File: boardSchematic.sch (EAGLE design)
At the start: 61 parts, among them IC2 TP4056, Q1 BC817-40SMD, Q2 BC817-40SMD, Q3 BC817-40SMD

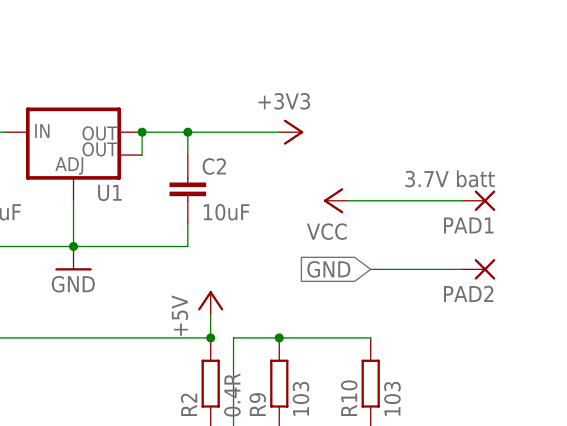
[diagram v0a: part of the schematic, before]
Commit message: Added on/off switch
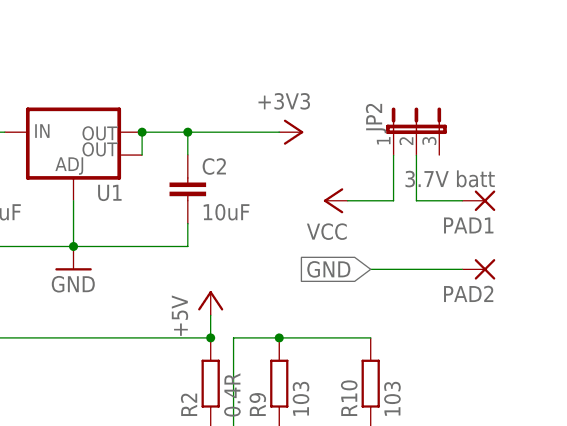
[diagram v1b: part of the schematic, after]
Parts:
- added JP2: (no value), jumper:JP2E
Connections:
- new net N$28: JP2.2, PAD1.P
- net VCC: now also JP2.1; no longer PAD1.P
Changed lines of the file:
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@@
 <part name="R24" library="rcl" deviceset="R-EU_" device="R0805" value="103"/>
 <part name="R27" library="rcl" deviceset="R-EU_" device="R0805" value="103"/>
+<part name="JP2" library="jumper" deviceset="JP2E" device=""/>
 </parts>
 <sheets>
@@
 <instance part="R24" gate="G$1" x="109.22" y="-129.54" rot="R90"/>
 <instance part="R27" gate="G$1" x="172.72" y="-132.08" rot="R90"/>
+<instance part="JP2" gate="1" x="325.12" y="-7.62"/>
 </instances>
 <busses>
@@
 <net name="VCC" class="0">
 <segment>
-<pinref part="P+1" gate="VCC" pin="VCC"/>
-<pinref part="PAD1" gate="1" pin="P"/>
-<wire x1="317.5" y1="-15.24" x2="330.2" y2="-15.24" width="0.1524" layer="91"/>
-</segment>
-<segment>
 <pinref part="U1" gate="G$1" pin="IN"/>
 <pinref part="C1" gate="G$1" pin="1"/>
@@
 <junction x="68.58" y="-99.06"/>
 </segment>
+<segment>
+<pinref part="P+1" gate="VCC" pin="VCC"/>
+<pinref part="JP2" gate="1" pin="1"/>
+<wire x1="317.5" y1="-15.24" x2="322.58" y2="-15.24" width="0.1524" layer="91"/>
+<wire x1="322.58" y1="-15.24" x2="322.58" y2="-10.16" width="0.1524" layer="91"/>
+</segment>
 </net>
 <net name="+5V" class="0">
@@
 </segment>
 </net>
+<net name="N$28" class="0">
+<segment>
+<pinref part="JP2" gate="1" pin="2"/>
+<wire x1="325.12" y1="-10.16" x2="325.12" y2="-15.24" width="0.1524" layer="91"/>
+<pinref part="PAD1" gate="1" pin="P"/>
+<wire x1="325.12" y1="-15.24" x2="330.2" y2="-15.24" width="0.1524" layer="91"/>
+</segment>
+</net>

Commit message: First guess of routing
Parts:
- removed LED1: RD, led:LEDSML0805
- removed LED2, LED4: GR, led:LEDSML0805
- removed R10, R9: 103, rcl:R-EU_R0805
- removed R19, R20, R21, R23: 102, rcl:R-EU_R0805
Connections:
- removed net N$1: Q2.B, R21.2
- removed net N$10: IC2.STDBY, LED2.C
- removed net N$2: LED1.A, R9.1
- removed net N$21: Q3.B, R23.2
- removed net N$26: LED4.A, R20.1
- removed net N$29: MEGA328.PD4(T0/XCK/PCINT20), R20.2
- removed net N$4: Q1.B, R19.2
- removed net N$6: LED2.A, R10.1
- removed net N$8: IC2.CHRG, LED1.C
- net BZR: now also Q3.B; no longer R23.1
- net GND: no longer LED4.C
- net GR: now also Q2.B; no longer R21.1
- net N$14: no longer R10.2, R9.2
- net RD: now also Q1.B; no longer R19.1
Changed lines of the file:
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@@
 <part name="R2" library="rcl" deviceset="R-EU_" device="R1210W" value="0.4R"/>
 <part name="R8" library="rcl" deviceset="R-EU_" device="R0805" value="122"/>
-<part name="R9" library="rcl" deviceset="R-EU_" device="R0805" value="103"/>
-<part name="R10" library="rcl" deviceset="R-EU_" device="R0805" value="103"/>
 <part name="C4" library="rcl" deviceset="C-EU" device="C1210" value="10uF"/>
 <part name="C5" library="rcl" deviceset="C-EU" device="C1210" value="10uF"/>
-<part name="LED1" library="led" deviceset="LED" device="SML0805" value="RD"/>
-<part name="LED2" library="led" deviceset="LED" device="SML0805" value="GR"/>
 <part name="GND5" library="supply1" deviceset="GND" device=""/>
 <part name="RF" library="pinhead" deviceset="PINHD-2X4" device=""/>
@@
 <part name="R14" library="rcl" deviceset="R-US_" device="R0805" value="103"/>
 <part name="BEACON" library="frankduerr" deviceset="MOD-NRF8001" device="MOD-NRF8001"/>
-<part name="R20" library="rcl" deviceset="R-EU_" device="R0805" value="102"/>
-<part name="LED4" library="led" deviceset="LED" device="SML0805" value="GR"/>
-<part name="GND4" library="supply1" deviceset="GND" device=""/>
 <part name="LED3" library="led" deviceset="Z-POWER-LED" device=""/>
 <part name="LED5" library="led" deviceset="Z-POWER-LED" device=""/>
@@
 <part name="R17" library="rcl" deviceset="R-EU_" device="R1206" value="1R0"/>
 <part name="R18" library="rcl" deviceset="R-EU_" device="R1206" value="1R0"/>
-<part name="R19" library="rcl" deviceset="R-EU_" device="R0805" value="102"/>
-<part name="R21" library="rcl" deviceset="R-EU_" device="R0805" value="102"/>
 <part name="Q1" library="transistor-npn" deviceset="BC817*" device="SMD" technology="-40"/>
 <part name="Q2" library="transistor-npn" deviceset="BC817*" device="SMD" technology="-40"/>
@@
 <part name="P+2" library="supply1" deviceset="VCC" device=""/>
 <part name="SG1" library="buzzer" deviceset="F/HMB" device=""/>
-<part name="R23" library="rcl" deviceset="R-EU_" device="R0805" value="102"/>
 <part name="Q3" library="transistor-npn" deviceset="BC817*" device="SMD" technology="-40"/>
 <part name="U$2" library="SparkFun-AnalogIC" deviceset="LM393" device=""/>
@@
 <instance part="R2" gate="G$1" x="302.26" y="-35.56" rot="R90"/>
 <instance part="R8" gate="G$1" x="269.24" y="-66.04" rot="R90"/>
-<instance part="R9" gate="G$1" x="309.88" y="-35.56" rot="R90"/>
-<instance part="R10" gate="G$1" x="320.04" y="-35.56" rot="R90"/>
 <instance part="C4" gate="G$1" x="314.96" y="-66.04"/>
 <instance part="C5" gate="G$1" x="304.8" y="-66.04"/>
-<instance part="LED1" gate="G$1" x="309.88" y="-45.72"/>
-<instance part="LED2" gate="G$1" x="320.04" y="-45.72"/>
 <instance part="GND5" gate="1" x="264.16" y="-81.28"/>
 <instance part="RF" gate="A" x="139.7" y="-83.82"/>
@@
 <instance part="R14" gate="G$1" x="119.38" y="-83.82"/>
 <instance part="BEACON" gate="G$1" x="182.88" y="-33.02"/>
-<instance part="R20" gate="G$1" x="91.44" y="-43.18" rot="R180"/>
-<instance part="LED4" gate="G$1" x="101.6" y="-43.18" rot="R90"/>
-<instance part="GND4" gate="1" x="109.22" y="-48.26"/>
 <instance part="LED3" gate="G$1" x="22.86" y="-119.38"/>
 <instance part="LED5" gate="G$1" x="38.1" y="-119.38"/>
@@
 <instance part="R17" gate="G$1" x="53.34" y="-109.22" rot="R270"/>
 <instance part="R18" gate="G$1" x="68.58" y="-109.22" rot="R270"/>
-<instance part="R19" gate="G$1" x="12.7" y="-134.62"/>
-<instance part="R21" gate="G$1" x="12.7" y="-149.86"/>
 <instance part="Q1" gate="G$1" x="58.42" y="-134.62"/>
 <instance part="Q2" gate="G$1" x="27.94" y="-149.86"/>
@@
 <instance part="P+2" gate="VCC" x="53.34" y="-91.44"/>
 <instance part="SG1" gate="G$1" x="86.36" y="-111.76" rot="R270"/>
-<instance part="R23" gate="G$1" x="12.7" y="-142.24"/>
 <instance part="Q3" gate="G$1" x="81.28" y="-142.24"/>
 <instance part="U$2" gate="G1" x="139.7" y="-137.16"/>
@@
 <wire x1="167.64" y1="-30.48" x2="157.48" y2="-30.48" width="0.1524" layer="91"/>
 <label x="157.48" y="-30.48" size="1.778" layer="95"/>
-</segment>
-<segment>
-<pinref part="LED4" gate="G$1" pin="C"/>
-<pinref part="GND4" gate="1" pin="GND"/>
-<wire x1="109.22" y1="-43.18" x2="106.68" y2="-43.18" width="0.1524" layer="91"/>
-<wire x1="109.22" y1="-45.72" x2="109.22" y2="-43.18" width="0.1524" layer="91"/>
-<junction x="109.22" y="-43.18"/>
 </segment>
 <segment>
@@
 </segment>
 </net>
-<net name="N$2" class="0">
-<segment>
-<pinref part="LED1" gate="G$1" pin="A"/>
-<pinref part="R9" gate="G$1" pin="1"/>
-<wire x1="309.88" y1="-43.18" x2="309.88" y2="-40.64" width="0.1524" layer="91"/>
-</segment>
-</net>
-<net name="N$6" class="0">
-<segment>
-<pinref part="LED2" gate="G$1" pin="A"/>
-<pinref part="R10" gate="G$1" pin="1"/>
-<wire x1="320.04" y1="-43.18" x2="320.04" y2="-40.64" width="0.1524" layer="91"/>
-</segment>
-</net>
-<net name="N$8" class="0">
-<segment>
-<pinref part="IC2" gate="G$1" pin="CHRG"/>
-<pinref part="LED1" gate="G$1" pin="C"/>
-<wire x1="302.26" y1="-50.8" x2="309.88" y2="-50.8" width="0.1524" layer="91"/>
-</segment>
-</net>
-<net name="N$10" class="0">
-<segment>
-<pinref part="IC2" gate="G$1" pin="STDBY"/>
-<pinref part="LED2" gate="G$1" pin="C"/>
-<wire x1="302.26" y1="-53.34" x2="320.04" y2="-53.34" width="0.1524" layer="91"/>
-<wire x1="320.04" y1="-53.34" x2="320.04" y2="-50.8" width="0.1524" layer="91"/>
-</segment>
-</net>
 <net name="N$14" class="0">
 <segment>
-<pinref part="R10" gate="G$1" pin="2"/>
-<pinref part="R9" gate="G$1" pin="2"/>
-<wire x1="320.04" y1="-30.48" x2="309.88" y2="-30.48" width="0.1524" layer="91"/>
-<wire x1="309.88" y1="-30.48" x2="304.8" y2="-30.48" width="0.1524" layer="91"/>
-<wire x1="304.8" y1="-30.48" x2="304.8" y2="-48.26" width="0.1524" layer="91"/>
-<junction x="309.88" y="-30.48"/>
 <pinref part="IC2" gate="G$1" pin="CE"/>
 <pinref part="R2" gate="G$1" pin="1"/>
@@
 <wire x1="274.32" y1="-60.96" x2="304.8" y2="-60.96" width="0.1524" layer="91"/>
 <wire x1="304.8" y1="-60.96" x2="304.8" y2="-48.26" width="0.1524" layer="91"/>
-<junction x="304.8" y="-48.26"/>
 <pinref part="C5" gate="G$1" pin="1"/>
 <wire x1="304.8" y1="-60.96" x2="304.8" y2="-63.5" width="0.1524" layer="91"/>
@@
 <wire x1="198.12" y1="-25.4" x2="203.2" y2="-25.4" width="0.1524" layer="91"/>
 <label x="203.2" y="-25.4" size="1.778" layer="95"/>
-</segment>
-</net>
-<net name="N$26" class="0">
-<segment>
-<pinref part="LED4" gate="G$1" pin="A"/>
-<pinref part="R20" gate="G$1" pin="1"/>
-<wire x1="99.06" y1="-43.18" x2="96.52" y2="-43.18" width="0.1524" layer="91"/>
-</segment>
-</net>
-<net name="N$29" class="0">
-<segment>
-<pinref part="MEGA328" gate="1" pin="PD4(T0/XCK/PCINT20)"/>
-<pinref part="R20" gate="G$1" pin="2"/>
-<wire x1="78.74" y1="-43.18" x2="86.36" y2="-43.18" width="0.1524" layer="91"/>
-</segment>
-</net>
-<net name="N$1" class="0">
-<segment>
-<pinref part="R21" gate="G$1" pin="2"/>
-<pinref part="Q2" gate="G$1" pin="B"/>
-<wire x1="17.78" y1="-149.86" x2="25.4" y2="-149.86" width="0.1524" layer="91"/>
-</segment>
-</net>
-<net name="N$4" class="0">
-<segment>
-<pinref part="R19" gate="G$1" pin="2"/>
-<pinref part="Q1" gate="G$1" pin="B"/>
-<wire x1="17.78" y1="-134.62" x2="55.88" y2="-134.62" width="0.1524" layer="91"/>
 </segment>
 </net>
@@
 <net name="GR" class="0">
 <segment>
-<pinref part="R21" gate="G$1" pin="1"/>
-<wire x1="7.62" y1="-149.86" x2="2.54" y2="-149.86" width="0.1524" layer="91"/>
 <label x="2.54" y="-149.86" size="1.778" layer="95" rot="R180" xref="yes"/>
+<pinref part="Q2" gate="G$1" pin="B"/>
+<wire x1="2.54" y1="-149.86" x2="25.4" y2="-149.86" width="0.1524" layer="91"/>
 </segment>
 </net>
 <net name="RD" class="0">
 <segment>
-<pinref part="R19" gate="G$1" pin="1"/>
-<wire x1="7.62" y1="-134.62" x2="2.54" y2="-134.62" width="0.1524" layer="91"/>
 <label x="2.54" y="-134.62" size="1.778" layer="95" rot="R180" xref="yes"/>
-</segment>
-</net>
-<net name="N$21" class="0">
-<segment>
-<pinref part="R23" gate="G$1" pin="2"/>
-<pinref part="Q3" gate="G$1" pin="B"/>
-<wire x1="17.78" y1="-142.24" x2="78.74" y2="-142.24" width="0.1524" layer="91"/>
+<pinref part="Q1" gate="G$1" pin="B"/>
+<wire x1="2.54" y1="-134.62" x2="55.88" y2="-134.62" width="0.1524" layer="91"/>
 </segment>
 </net>
@@
 <net name="BZR" class="0">
 <segment>
-<pinref part="R23" gate="G$1" pin="1"/>
-<wire x1="7.62" y1="-142.24" x2="2.54" y2="-142.24" width="0.1524" layer="91"/>
 <label x="2.54" y="-142.24" size="1.778" layer="95" rot="R180" xref="yes"/>
-</segment>
-</net>
+<pinref part="Q3" gate="G$1" pin="B"/>
+<wire x1="2.54" y1="-142.24" x2="78.74" y2="-142.24" width="0.1524" layer="91"/>
+</segment>
+</net>
